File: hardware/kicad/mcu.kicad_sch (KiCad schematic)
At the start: 58 parts, among them J3 SWD, J4 USB-C, SW1 BOOTSEL, SW2 RESET, U3 RP2040, U4 W25Q16JVSS, U5 AP2112K-3.3, U6 74LVC1G00, U7 74AHCT1G08, U8 74AHCT1G08, Y1 12MHz

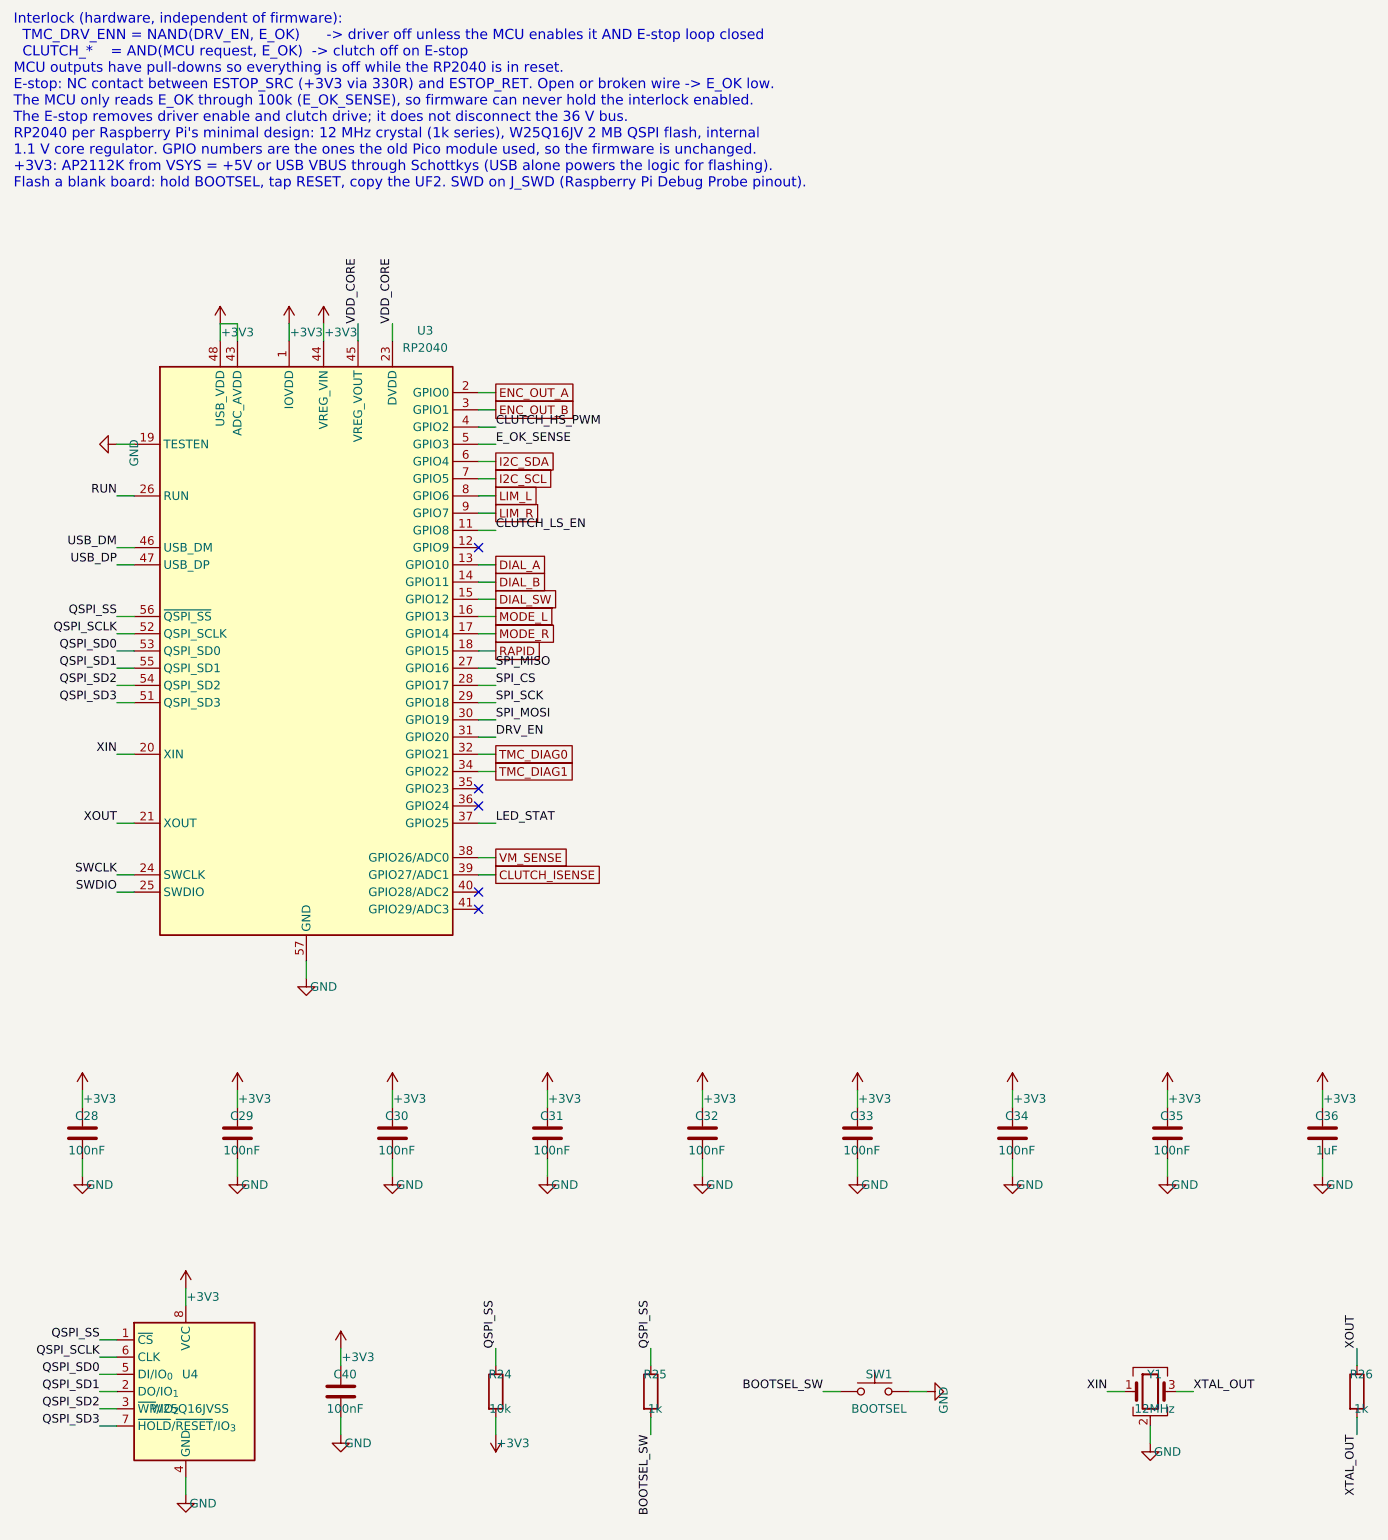
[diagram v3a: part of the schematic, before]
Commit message: RP2040 parts after LCSC check: W25Q128JVSIQ (C113767, W25Q16 out of stock), ABM8-272-T3 (C20625731), SWD on a 0.1in header (JST-SH out of stock)
Co-Authored-By: Claude Opus 5.5 <noreply@anthropic.com>
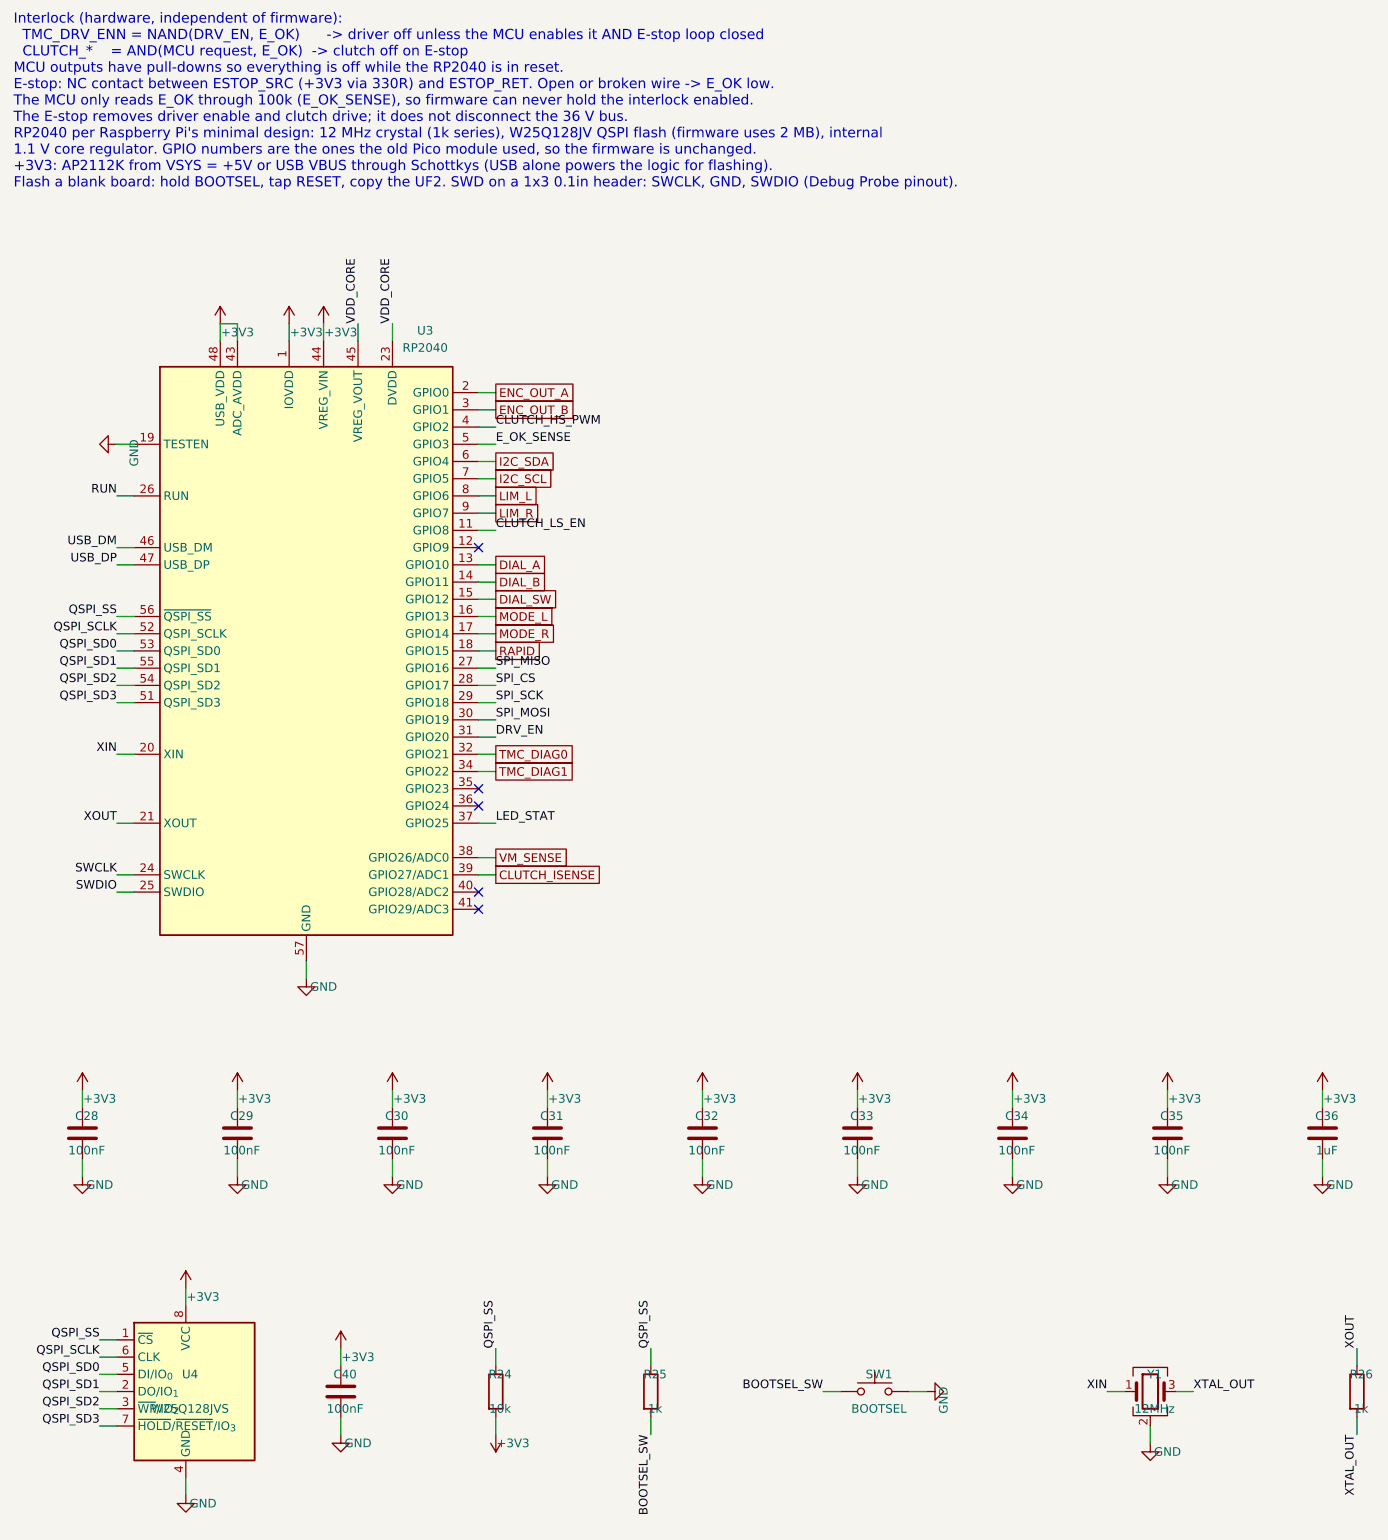
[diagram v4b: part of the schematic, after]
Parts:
- J3: footprint Connector_JST:JST_SH_SM03B-SRSS-TB_1x03-1MP_P1.00mm_Horizontal -> Connector_PinHeader_2.54mm:PinHeader_1x03_P2.54mm_Vertical; LCSC C160403 -> (none); MPN JST SM03B-SRSS-TB(LF)(SN) -> 2.54 mm 1x3 male header, hand-solder (Debug Probe's JST-to-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
- U4: value W25Q16JVSS -> W25Q128JVS; symbol Memory_Flash:W25Q16JVSS -> Memory_Flash:W25Q128JVS; LCSC (none) -> C113767; MPN Winbond W25Q16JVSSIQ -> Winbond W25Q128JVSIQ (W25Q16 is out of stock; firmware uses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
- Y1: LCSC (none) -> C20625731; MPN Abracon ABM8-272-T3 (12 MHz, CL 10 pF) -> Abracon ABM8-272-T3 (12 MHz, CL 10 pF, ESR 50R; RPi-approve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
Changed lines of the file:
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@@
 		(company "Mill power feed controller")
 	)
-	(text "Interlock (hardware, independent of firmware):\n  TMC_DRV_ENN = NAND(DRV_EN, E_OK)      -> driver off unless the MCU enables it AND E-stop loop closed\n  CLUTCH_*    = AND(MCU request, E_OK)  -> clutch off on E-stop\nMCU outputs have pull-downs so everything is off while the RP2040 is in reset.\nE-stop: NC contact between ESTOP_SRC (+3V3 via 330R) and ESTOP_RET. Open or broken wire -> E_OK low.\nThe MCU only reads E_OK through 100k (E_OK_SENSE), so firmware can never hold the interlock enabled.\nThe E-stop removes driver enable and clutch drive; it does not disconnect the 36 V bus.\nRP2040 per Raspberry Pi's minimal design: 12 MHz crystal (1k series), W25Q16JV 2 MB QSPI flash, internal\n1.1 V core regulator. GPIO numbers are the ones the old Pico module used, so the firmware is unchanged.\n+3V3: AP2112K from VSYS = +5V or USB VBUS through Schottkys (USB alone powers the logic for flashing).\nFlash a blank board: hold BOOTSEL, tap RESET, copy the UF2. SWD on J_SWD (Raspberry Pi Debug Probe pinout)."
+	(text "Interlock (hardware, independent of firmware):\n  TMC_DRV_ENN = NAND(DRV_EN, E_OK)      -> driver off unless the MCU enables it AND E-stop loop closed\n  CLUTCH_*    = AND(MCU request, E_OK)  -> clutch off on E-stop\nMCU outputs have pull-downs so everything is off while the RP2040 is in reset.\nE-stop: NC contact between ESTOP_SRC (+3V3 via 330R) and ESTOP_RET. Open or broken wire -> E_OK low.\nThe MCU only reads E_OK through 100k (E_OK_SENSE), so firmware can never hold the interlock enabled.\nThe E-stop removes driver enable and clutch drive; it does not disconnect the 36 V bus.\nRP2040 per Raspberry Pi's minimal design: 12 MHz crystal (1k series), W25Q128JV QSPI flash (firmware uses 2 MB), internal\n1.1 V core regulator. GPIO numbers are the ones the old Pico module used, so the firmware is unchanged.\n+3V3: AP2112K from VSYS = +5V or USB VBUS through Schottkys (USB alone powers the logic for flashing).\nFlash a blank board: hold BOOTSEL, tap RESET, copy the UF2. SWD on a 1x3 0.1in header: SWCLK, GND, SWDIO (Debug Probe pinout)."
 		(exclude_from_sim no)
 		(at 20.32 30.48 0)
@@
 	)
 	(symbol
-		(lib_id "Memory_Flash:W25Q16JVSS")
+		(lib_id "Memory_Flash:W25Q128JVS")
 		(at 45.72 233.68 0)
 		(unit 1)
@@
 			)
 		)
-		(property "Value" "W25Q16JVSS"
+		(property "Value" "W25Q128JVS"
 			(at 46.355 236.22 0)
 			(effects
@@
 			)
 		)
-		(property "MPN" "Winbond W25Q16JVSSIQ"
+		(property "MPN" "Winbond W25Q128JVSIQ (W25Q16 is out of stock; firmware uses the first 2 MB)"
 			(at 45.72 233.68 0)
 			(effects
@@
 			)
 		)
-		(property "LCSC" ""
+		(property "LCSC" "C113767"
 			(at 45.72 233.68 0)
 			(effects
@@
 			)
 		)
-		(property "MPN" "Abracon ABM8-272-T3 (12 MHz, CL 10 pF)"
+		(property "MPN" "Abracon ABM8-272-T3 (12 MHz, CL 10 pF, ESR 50R; RPi-approved)"
 			(at 187.96 233.68 0)
 			(effects
@@
 			)
 		)
-		(property "LCSC" ""
+		(property "LCSC" "C20625731"
 			(at 187.96 233.68 0)
 			(effects
@@
 			)
 		)
-		(property "Footprint" "Connector_JST:JST_SH_SM03B-SRSS-TB_1x03-1MP_P1.00mm_Horizontal"
+		(property "Footprint" "Connector_PinHeader_2.54mm:PinHeader_1x03_P2.54mm_Vertical"
 			(at 88.9 271.78 0)
 			(effects
@@
 			)
 		)
-		(property "MPN" "JST SM03B-SRSS-TB(LF)(SN)"
+		(property "MPN" "2.54 mm 1x3 male header, hand-solder (Debug Probe's JST-to-0.1in cable)"
 			(at 88.9 271.78 0)
 			(effects
@@
 			)
 		)
-		(property "LCSC" "C160403"
+		(property "LCSC" ""
 			(at 88.9 271.78 0)
 			(effects

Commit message: Schematic: 100 nF right at RP2040 DVDD pin 23 and USBLC6-2SC6 ESD (C7519) on the USB-C lines (PCB review round 2)
Co-Authored-By: Claude Opus 5.5 <noreply@anthropic.com>
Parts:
- added C49: 100nF, Capacitor_SMD:C_0603_1608Metric, symbol Device:C
- added U9: 74AHCT1G08, Package_TO_SOT_SMD:SOT-23-5, symbol 74xGxx:74AHCT1G08
- C41: value 15pF -> 100nF; LCSC C1644 -> C14663; MPN Samsung CL10C150JB8NNNC -> Yageo CC0603KRX7R9BB104
- C43: value 1uF -> 15pF; LCSC C15849 -> C1644; MPN Samsung CL10A105KB8NNNC -> Samsung CL10C150JB8NNNC
- C44: value 4.7uF 10V -> 1uF; footprint Capacitor_SMD:C_0805_2012Metric -> Capacitor_SMD:C_0603_1608Metric; LCSC C1779 -> C15849; MPN Samsung CL21A475KAQNNNE -> Samsung CL10A105KB8NNNC
- C45: value 100nF -> 4.7uF 10V; footprint Capacitor_SMD:C_0603_1608Metric -> Capacitor_SMD:C_0805_2012Metric; LCSC C14663 -> C1779; MPN Yageo CC0603KRX7R9BB104 -> Samsung CL21A475KAQNNNE
- U5: value AP2112K-3.3 -> USBLC6-2SC6; footprint Package_TO_SOT_SMD:SOT-23-5 -> Package_TO_SOT_SMD:SOT-23-6; symbol Regulator_Linear:AP2112K-3.3 -> Power_Protection:USBLC6-2SC6; LCSC C51118 -> C7519; MPN Diodes AP2112K-3.3TRG1 -> STMicroelectronics USBLC6-2SC6
- U6: value 74LVC1G00 -> AP2112K-3.3; symbol 74xGxx:74LVC1G00 -> Regulator_Linear:AP2112K-3.3; LCSC C7826 -> C51118; MPN SN74LVC1G00DBVR -> Diodes AP2112K-3.3TRG1
- U7: value 74AHCT1G08 -> 74LVC1G00; symbol 74xGxx:74AHCT1G08 -> 74xGxx:74LVC1G00; LCSC C113521 -> C7826; MPN SN74AHCT1G08DBVR -> SN74LVC1G00DBVR
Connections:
- net +3V3: now also C41.1, C46.1, U7.5 (VCC); no longer C40.1, C44.1, U5.5 (VOUT)
- net +5V: now also C48.1, U9.5 (VCC); no longer C46.1, U7.5 (VCC)
- net CLUTCH_HS_DRV: now also U9.4; no longer U8.4
- net CLUTCH_HS_PWM: now also U9.1; no longer U8.1
- net CLUTCH_LS_EN: now also U8.1; no longer U7.1
- net CLUTCH_LS_GATE: now also U8.4; no longer U7.4
- net DRV_EN: now also U7.1; no longer U6.1
- net E_OK: now also C49.1, U9.2; no longer C48.1, U6.2
- net GND: now also U6.2 (GND), C49.2, U9.3 (GND); no longer U6.3 (GND)
- net TMC_DRV_ENN: now also U7.4; no longer U6.4
- net USB_CONN_DM: now also U5.3 (I/O2), U5.4 (I/O2)
- net USB_CONN_DP: now also U5.1 (I/O1), U5.6 (I/O1)
- net VBUS: now also U5.5 (VBUS)
- net VDD_CORE: now also C40.1
- net VSYS: now also C44.1, U6.1 (VIN), U6.3 (EN); no longer C43.1, U5.1 (VIN), U5.3 (EN)
- net XIN: now also C42.1; no longer C41.1
- net XTAL_OUT: now also C43.1; no longer C42.1
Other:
- moved on the sheet: C40, C41, C42, C43, C44, C45, C46, C47, C48, D5, D6, U8
